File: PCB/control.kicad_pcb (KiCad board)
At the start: 2 copper layers, 86 x 50 mm, 9 parts, among them P1 CONN_01X07, P13 CONN_01X07, P14 CONN_01X04, P5 BATTERY, P8 CONN_01X04, U1 4056_CARG

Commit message: Fix PCBs
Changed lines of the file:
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@@
-(kicad_pcb (version 4) (host pcbnew 4.0.0-rc1-stable)
+(kicad_pcb (version 4) (host pcbnew 4.0.2+dfsg1-stable)
   (general
     (links 29)
-    (no_connects 2)
-    (area 37.351725 28.448816 278.178572 182.950001)
+    (no_connects 0)
+    (area 84.474999 53.824999 170.575001 103.975001)
     (thickness 1.6)
     (drawings 32)
@@
   (module 4056_lipoCharg (layer F.Cu)
     (at 89.8 77.4)
-    (fp_text reference U1 (at 0 0.5) (layer F.SilkS)
-      (effects (font (size 1 1) (thickness 0.15)))
-    )
-    (fp_text value 4056_CARG (at 0 -0.5) (layer F.Fab)
+    (fp_text reference U1 (at 6 3.4) (layer F.SilkS)
+      (effects (font (size 1 1) (thickness 0.15)))
+    )
+    (fp_text value 4056_CARG (at 9.4 6.4) (layer F.SilkS)
       (effects (font (size 1 1) (thickness 0.15)))
     )
@@
     (at 121.66 66.3 270)
     (descr ABK-PRO-MINI)
-    (fp_text reference RAW1 (at 0 0 270) (layer F.SilkS)
+    (fp_text reference RAW1 (at 2.9 10.86 360) (layer F.Fab)
       (effects (font (thickness 0.15)))
     )
-    (fp_text value ARDUPROMINI (at 0 0 270) (layer F.SilkS)
+    (fp_text value ARDUPROMINI (at -0.3 8.46 360) (layer F.SilkS)
       (effects (font (thickness 0.15)))
     )
@@
     (descr "Through hole pin header")
     (tags "pin header")
-    (fp_text reference P1 (at 0 -5.1 90) (layer F.SilkS)
+    (fp_text reference P1 (at -0.1 -2.8 90) (layer F.SilkS)
       (effects (font (size 1 1) (thickness 0.15)))
     )
@@
     (descr "Through hole pin header")
     (tags "pin header")
-    (fp_text reference P5 (at 0 -5.1) (layer F.SilkS)
-      (effects (font (size 1 1) (thickness 0.15)))
-    )
-    (fp_text value BATTERY (at 0 -3.1) (layer F.Fab)
+    (fp_text reference P5 (at 0.25 -2.75) (layer F.SilkS)
+      (effects (font (size 1 1) (thickness 0.15)))
+    )
+    (fp_text value BATTERY (at -1.95 3.25 90) (layer F.Fab)
       (effects (font (size 1 1) (thickness 0.15)))
     )
@@
     (descr "Through hole pin header")
     (tags "pin header")
-    (fp_text reference P8 (at 0 -5.1) (layer F.SilkS)
+    (fp_text reference P8 (at -0.15 -2.85) (layer F.SilkS)
       (effects (font (size 1 1) (thickness 0.15)))
     )
@@
     (descr "Through hole pin header")
     (tags "pin header")
-    (fp_text reference P13 (at 0 -5.1) (layer F.SilkS)
+    (fp_text reference P13 (at 0 -2.44) (layer F.SilkS)
       (effects (font (size 1 1) (thickness 0.15)))
     )
@@
     (descr "Through hole pin header")
     (tags "pin header")
-    (fp_text reference P14 (at 0 -5.1 270) (layer F.SilkS)
+    (fp_text reference P14 (at 0 -2.68 270) (layer F.SilkS)
       (effects (font (size 1 1) (thickness 0.15)))
     )
@@
     (descr "Capacitor 6mm Disc, Pitch 5mm")
     (tags Capacitor)
-    (fp_text reference C2 (at 2.5 -3.5) (layer F.SilkS)
+    (fp_text reference C2 (at 4.95 -2.85) (layer F.SilkS)
       (effects (font (size 1 1) (thickness 0.15)))
     )
@@
   (segment (start 129.1 54.95) (end 129.25 55.1) (width 0.25) (layer B.Cu) (net 1))
   (segment (start 114.35 54.95) (end 129.1 54.95) (width 0.25) (layer B.Cu) (net 1))
-  (segment (start 112.8 56.5) (end 114.35 54.95) (width 0.25) (layer B.Cu) (net 1) (status 400000))
-  (segment (start 112.8 56.9) (end 112.8 56.5) (width 0.25) (layer B.Cu) (net 1) (status C00000))
+  (segment (start 112.8 56.5) (end 114.35 54.95) (width 0.25) (layer B.Cu) (net 1))
+  (segment (start 112.8 56.9) (end 112.8 56.5) (width 0.25) (layer B.Cu) (net 1))
   (segment (start 90 82.4824) (end 90 77.7) (width 0.25) (layer F.Cu) (net 1))
   (segment (start 90 77.7) (end 92.05 75.65) (width 0.25) (layer F.Cu) (net 1))

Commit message: Add logo ElectronicCats
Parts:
- added G***: LOGO, theinventorhouse:electronic_cats_logo_8x6, F.Cu at (94.0, 66.3)

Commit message: Fix bug GND of GY-87
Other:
- board size 86 x 50 mm -> 50 x 50 mm
- board text added: "+"
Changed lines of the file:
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@@
-(kicad_pcb (version 4) (host pcbnew 4.0.2+dfsg1-stable)
+(kicad_pcb (version 4) (host pcbnew 4.0.0-rc1-stable)
   (general
-    (links 0)
+    (links 29)
     (no_connects 0)
-    (area 84.474999 53.824999 170.575001 103.975001)
+    (area 73.387672 42.3 175.364286 110.100001)
     (thickness 1.6)
-    (drawings 32)
+    (drawings 27)
     (tracks 165)
     (zones 0)
@@
     (descr "Through hole pin header")
     (tags "pin header")
-    (fp_text reference P5 (at 0.25 -2.75) (layer F.SilkS)
-      (effects (font (size 1 1) (thickness 0.15)))
-    )
-    (fp_text value BATTERY (at -1.95 3.25 90) (layer F.Fab)
+    (fp_text reference P5 (at 0.7 4.55) (layer F.SilkS)
+      (effects (font (size 1 1) (thickness 0.15)))
+    )
+    (fp_text value BATTERY (at -1.95 3.05 90) (layer F.Fab)
       (effects (font (size 1 1) (thickness 0.15)))
     )
@@
       (xy 1.899124 -3.352032) (xy 1.924979 -3.352698) (xy 1.950789 -3.3528) (xy 1.989366 -3.352204)) (layer F.SilkS) (width 0.01))
   )
+  (gr_text "+\n" (at 130 77.75) (layer F.SilkS)
+    (effects (font (size 1.5 1.5) (thickness 0.3)))
+  )
   (dimension 11.5 (width 0.3) (layer Margin)
     (gr_text 11.500mm (at 124.8 70.3) (layer Margin)
@@
     (arrow2b (pts (xy 121.8 95.65) (xy 122.926504 95.063579)))
   )
-  (dimension 1 (width 0.3) (layer Margin)
-    (gr_text 1.000mm (at 170 104.65) (layer Margin)
-      (effects (font (size 1.5 1.5) (thickness 0.3)))
-    )
-    (feature1 (pts (xy 170.5 97.3) (xy 170.5 106)))
-    (feature2 (pts (xy 169.5 97.3) (xy 169.5 106)))
-    (crossbar (pts (xy 169.5 103.3) (xy 170.5 103.3)))
-    (arrow1a (pts (xy 170.5 103.3) (xy 169.373496 103.886421)))
-    (arrow1b (pts (xy 170.5 103.3) (xy 169.373496 102.713579)))
-    (arrow2a (pts (xy 169.5 103.3) (xy 170.626504 103.886421)))
-    (arrow2b (pts (xy 169.5 103.3) (xy 170.626504 102.713579)))
-  )
-  (dimension 2 (width 0.3) (layer Margin)
-    (gr_text 2.000mm (at 169.5 92.7) (layer Margin)
-      (effects (font (size 1.5 1.5) (thickness 0.3)))
-    )
-    (feature1 (pts (xy 170.5 97.3) (xy 170.5 91.35)))
-    (feature2 (pts (xy 168.5 97.3) (xy 168.5 91.35)))
-    (crossbar (pts (xy 168.5 94.05) (xy 170.5 94.05)))
-    (arrow1a (pts (xy 170.5 94.05) (xy 169.373496 94.636421)))
-    (arrow1b (pts (xy 170.5 94.05) (xy 169.373496 93.463579)))
-    (arrow2a (pts (xy 168.5 94.05) (xy 169.626504 94.636421)))
-    (arrow2b (pts (xy 168.5 94.05) (xy 169.626504 93.463579)))
-  )
-  (dimension 3.5 (width 0.3) (layer Margin)
-    (gr_text 3.500mm (at 157.5 92.7) (layer Margin)
-      (effects (font (size 1.5 1.5) (thickness 0.3)))
-    )
-    (feature1 (pts (xy 159.25 96.55) (xy 159.25 91.35)))
-    (feature2 (pts (xy 155.75 96.55) (xy 155.75 91.35)))
-    (crossbar (pts (xy 155.75 94.05) (xy 159.25 94.05)))
-    (arrow1a (pts (xy 159.25 94.05) (xy 158.123496 94.636421)))
-    (arrow1b (pts (xy 159.25 94.05) (xy 158.123496 93.463579)))
-    (arrow2a (pts (xy 155.75 94.05) (xy 156.876504 94.636421)))
-    (arrow2b (pts (xy 155.75 94.05) (xy 156.876504 93.463579)))
-  )
   (dimension 31.25 (width 0.3) (layer Margin)
     (gr_text 31.250mm (at 146.4 69.525 90) (layer Margin)
@@
     (arrow2a (pts (xy 80.101957 53.849745) (xy 79.515536 54.976249)))
     (arrow2b (pts (xy 80.101957 53.849745) (xy 80.688378 54.976249)))
-  )
-  (gr_circle (center 169.5 97.3) (end 170.5 97.3) (layer Edge.Cuts) (width 0.15))
-  (gr_circle (center 157.5 96.55) (end 159.25 96.55) (layer Edge.Cuts) (width 0.15))
-  (dimension 1.75 (width 0.3) (layer Margin)
-    (gr_text 1.750mm (at 158.375 104.65) (layer Margin)
-      (effects (font (size 1.5 1.5) (thickness 0.3)))
-    )
-    (feature1 (pts (xy 159.25 96.55) (xy 159.25 106)))
-    (feature2 (pts (xy 157.5 96.55) (xy 157.5 106)))
-    (crossbar (pts (xy 157.5 103.3) (xy 159.25 103.3)))
-    (arrow1a (pts (xy 159.25 103.3) (xy 158.123496 103.886421)))
-    (arrow1b (pts (xy 159.25 103.3) (xy 158.123496 102.713579)))
-    (arrow2a (pts (xy 157.5 103.3) (xy 158.626504 103.886421)))
-    (arrow2b (pts (xy 157.5 103.3) (xy 158.626504 102.713579)))
   )
   (gr_line (start 134.55 93.9) (end 134.55 53.9) (layer Edge.Cuts) (width 0.15))
@@
     (connect_pads (clearance 0.8))
     (min_thickness 0.254)
-    (fill (arc_segments 16) (thermal_gap 0.508) (thermal_bridge_width 0.508))
+    (fill yes (arc_segments 16) (thermal_gap 0.508) (thermal_bridge_width 0.508))
     (polygon
       (pts
@@
     (connect_pads (clearance 0.8))
     (min_thickness 0.254)
-    (fill (arc_segments 16) (thermal_gap 0.508) (thermal_bridge_width 0.508))
+    (fill yes (arc_segments 16) (thermal_gap 0.508) (thermal_bridge_width 0.508))
     (polygon
       (pts

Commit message: PCB final
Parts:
- added P0n1: ON, Pin_Headers:Pin_Header_Straight_1x02, F.Cu at (101.8, 96.4)
- moved D1 19.1 mm to (112.4, 97.7), turned to 90 degrees
- moved G*** 2.40 mm to (94.5, 64.0)
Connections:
- D1 pad 1: +BATT -> Net-(D1-Pad1)
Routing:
- net +BATT: track 87.3 -> 131.4 mm
- net Net-(D1-Pad1): track 0.00 -> 14.4 mm
- net Net-(D1-Pad2): track 42.2 -> 46.4 mm
- net S_TX: track 15.2 -> 16.0 mm
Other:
- net class BATT added: clearance 0.2, trace_width 0.5, via_dia 0.6, via_drill 0.4

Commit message: Fix details
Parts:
- added REF**: Symbol_OSHW-Logo_SilkScreen_BIG, Symbols:Symbol_OSHW-Logo_SilkScreen_BIG, B.Cu at (100.6, 64.8)
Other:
- board text added: "Main Board"

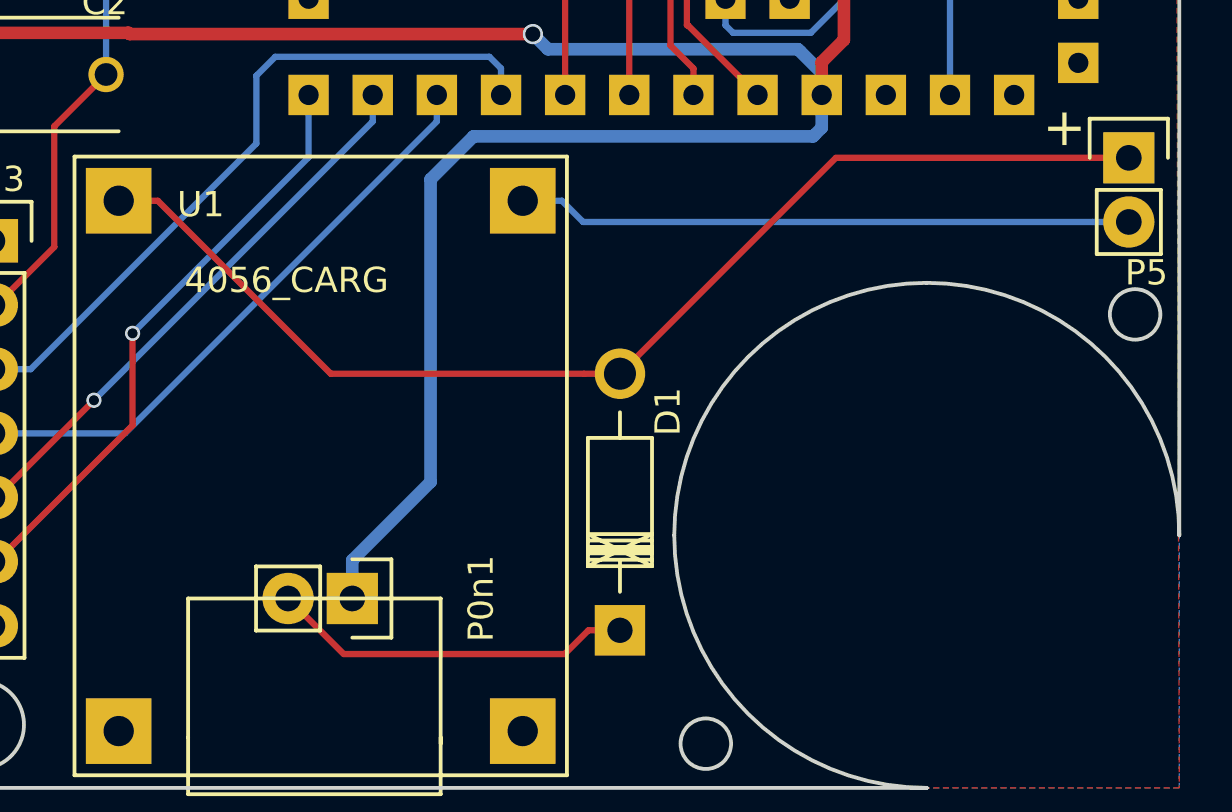
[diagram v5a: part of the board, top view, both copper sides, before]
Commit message: Fix Source Track
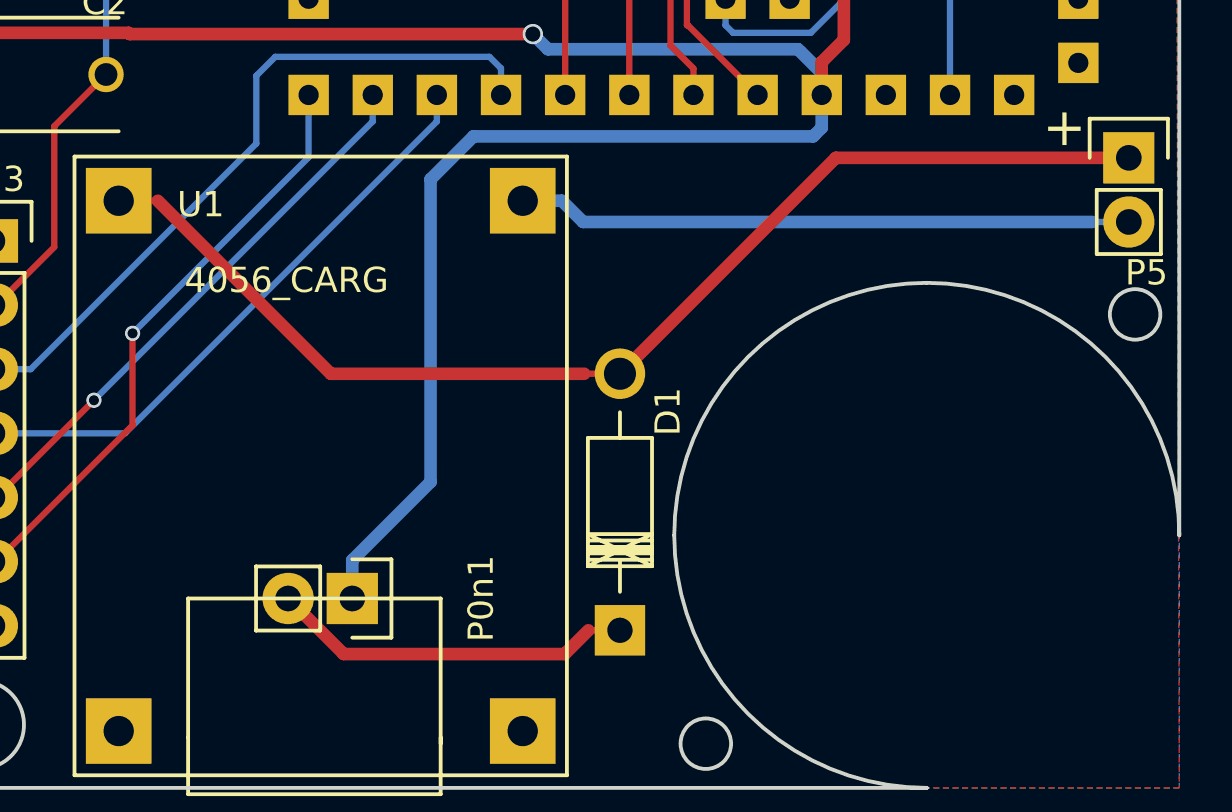
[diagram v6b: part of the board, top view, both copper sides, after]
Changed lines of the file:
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@@
   (layers
     (0 F.Cu signal)
-    (31 B.Cu signal)
+    (31 B.Cu signal hide)
     (32 B.Adhes user)
     (33 F.Adhes user)
@@
   (segment (start 87.55 84.78) (end 87.7024 84.78) (width 0.25) (layer F.Cu) (net 1))
   (segment (start 92.55 80.65) (end 94.1 80.65) (width 0.25) (layer F.Cu) (net 2))
-  (segment (start 94.1 80.65) (end 100.95 87.5) (width 0.25) (layer F.Cu) (net 2))
+  (segment (start 94.1 80.65) (end 100.95 87.5) (width 0.5) (layer F.Cu) (net 2))
   (segment (start 110.986508 87.5) (end 112.4 87.5) (width 0.25) (layer F.Cu) (net 2))
-  (segment (start 100.95 87.5) (end 110.986508 87.5) (width 0.25) (layer F.Cu) (net 2))
-  (segment (start 132.55 78.95) (end 120.95 78.95) (width 0.25) (layer F.Cu) (net 2))
-  (segment (start 120.95 78.95) (end 112.4 87.5) (width 0.25) (layer F.Cu) (net 2))
+  (segment (start 100.95 87.5) (end 110.986508 87.5) (width 0.5) (layer F.Cu) (net 2))
+  (segment (start 132.55 78.95) (end 120.95 78.95) (width 0.5) (layer F.Cu) (net 2))
+  (segment (start 120.95 78.95) (end 112.4 87.5) (width 0.5) (layer F.Cu) (net 2))
   (segment (start 104.9 79.8) (end 106.6 78.1) (width 0.5) (layer B.Cu) (net 3))
   (segment (start 120.09546 78.05454) (end 120.39 77.76) (width 0.5) (layer B.Cu) (net 3))
@@
   (segment (start 90.04 72.3) (end 100.07 62.27) (width 0.25) (layer B.Cu) (net 21))
   (segment (start 100.07 62.27) (end 100.07 61.22) (width 0.25) (layer B.Cu) (net 21))
-  (segment (start 108.55 80.65) (end 110.1 80.65) (width 0.25) (layer B.Cu) (net 22))
-  (segment (start 110.1 80.65) (end 110.94 81.49) (width 0.25) (layer B.Cu) (net 22))
-  (segment (start 110.94 81.49) (end 131.11316 81.49) (width 0.25) (layer B.Cu) (net 22))
+  (segment (start 108.55 80.65) (end 110.1 80.65) (width 0.5) (layer B.Cu) (net 22))
+  (segment (start 110.1 80.65) (end 110.94 81.49) (width 0.5) (layer B.Cu) (net 22))
+  (segment (start 110.94 81.49) (end 131.11316 81.49) (width 0.5) (layer B.Cu) (net 22))
   (segment (start 131.11316 81.49) (end 132.55 81.49) (width 0.25) (layer B.Cu) (net 22))
-  (segment (start 101.46 98.6) (end 110.21051 98.6) (width 0.25) (layer F.Cu) (net 36))
-  (segment (start 110.21051 98.6) (end 111.15051 97.66) (width 0.25) (layer F.Cu) (net 36))
+  (segment (start 101.46 98.6) (end 110.21051 98.6) (width 0.5) (layer F.Cu) (net 36))
+  (segment (start 110.21051 98.6) (end 111.15051 97.66) (width 0.5) (layer F.Cu) (net 36))
   (segment (start 111.15051 97.66) (end 112.4 97.66) (width 0.25) (layer F.Cu) (net 36))
-  (segment (start 99.26 96.4) (end 101.46 98.6) (width 0.25) (layer F.Cu) (net 36))
+  (segment (start 99.26 96.4) (end 101.46 98.6) (width 0.5) (layer F.Cu) (net 36))
   (zone (net 1) (net_name GND) (layer F.Cu) (hatch edge 0.508)
     (connect_pads (clearance 0.8))
